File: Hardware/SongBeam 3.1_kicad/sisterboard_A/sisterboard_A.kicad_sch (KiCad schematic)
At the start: 59 parts, among them J1 RJ45, J2 Conn_01x04, U1 PCMD3180IRTWR, U10 LP5907MFX-1.8_NOPB, U2 IM66D132H, U3 IM66D132H, U4 IM66D132H, U5 IM66D132H, U6 IM66D132H, U7 IM66D132H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

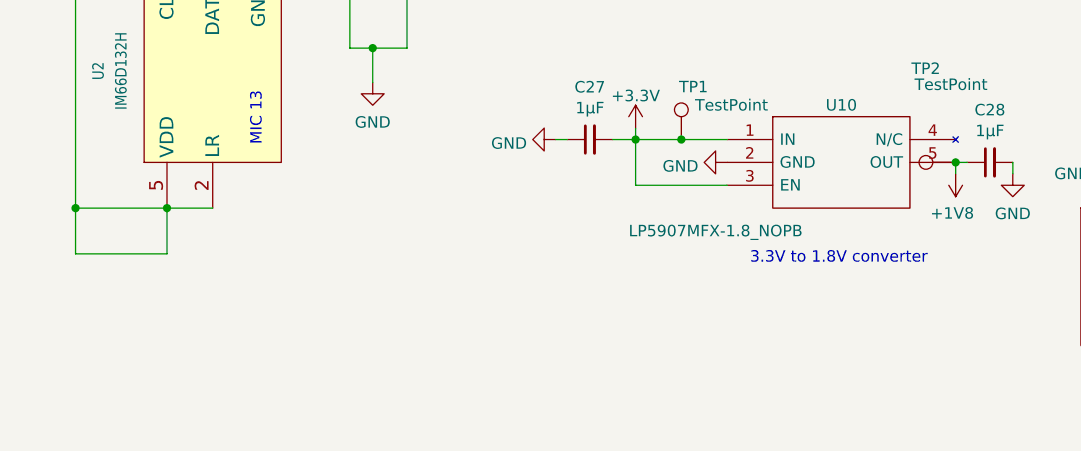
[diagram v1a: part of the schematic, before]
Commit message: Small tweaks, implementing the power modules
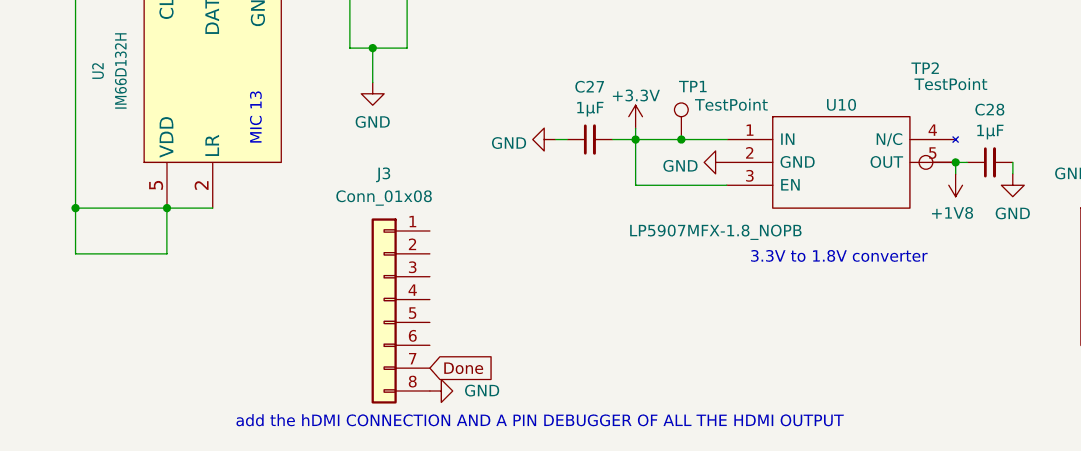
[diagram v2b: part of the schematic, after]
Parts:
- added J3: Conn_01x08, Connector_PinSocket_2.54mm:PinSocket_1x08_P2.54mm_Vertical, symbol Connector_Generic:Conn_01x08
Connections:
- net GND: now also J3.8 (Pin_8)
- new net Done: J3.7 (Pin_7)
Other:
- note added: "add the hDMI CONNECTION AND A PIN DEBUGGER OF ALL THE HDMI OUTPUT"
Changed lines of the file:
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@@
 		)
 	)
+	(text "add the hDMI CONNECTION AND A PIN DEBUGGER OF ALL THE HDMI OUTPUT\n"
+		(exclude_from_sim no)
+		(at 69.342 196.596 0)
+		(effects
+			(font
+				(size 1.27 1.27)
+			)
+		)
+	)
 	(text "MIC 11"
 		(exclude_from_sim no)
@@
 		)
 	)
+	(global_label "Done"
+		(shape input)
+		(at 57.15 190.5 0)
+		(fields_autoplaced yes)
+		(effects
+			(font
+				(size 1.27 1.27)
+			)
+			(justify left)
+		)
+		(property "Intersheetrefs" "${INTERSHEET_REFS}"
+			(at 64.7918 190.5 0)
+			(effects
+				(font
+					(size 1.27 1.27)
+				)
+				(justify left)
+				(hide yes)
+			)
+		)
+	)
 	(symbol
 		(lib_id "SoundRecorder_2.0:LP5907MFX-1.8_NOPB")
@@
 	)
 	(symbol
+		(lib_name "GND_2")
+		(lib_id "power:GND")
+		(at 57.15 193.04 90)
+		(unit 1)
+		(exclude_from_sim no)
+		(in_bom yes)
+		(on_board yes)
+		(dnp no)
+		(fields_autoplaced yes)
+		(property "Reference" "#PWR03"
+			(at 63.5 193.04 0)
+			(effects
+				(font
+					(size 1.27 1.27)
+				)
+				(hide yes)
+			)
+		)
+		(property "Value" "GND"
+			(at 60.96 193.0399 90)
+			(effects
+				(font
+					(size 1.27 1.27)
+				)
+				(justify right)
+			)
+		)
+		(property "Footprint" ""
+			(at 57.15 193.04 0)
+			(effects
+				(font
+					(size 1.27 1.27)
+				)
+				(hide yes)
+			)
+		)
+		(property "Datasheet" ""
+			(at 57.15 193.04 0)
+			(effects
+				(font
+					(size 1.27 1.27)
+				)
+				(hide yes)
+			)
+		)
+		(property "Description" "Power symbol creates a global label with name \"GND\" , ground"
+			(at 57.15 193.04 0)
+			(effects
+				(font
+					(size 1.27 1.27)
+				)
+				(hide yes)
+			)
+		)
+		(pin "1"
+		)
+		(instances
+			(project "sisterboard_A"
+				(path "/4ef09cdb-8bcc-4078-80cc-bd6392fd6a14"
+					(reference "#PWR03")
+					(unit 1)
+				)
+			)
+		)
+	)
+	(symbol
 		(lib_id "power:GND")
 		(at 137.16 54.61 90)
@@
 					(unit 1)
 				)
+			)
+		)
+	)
+	(symbol
+		(lib_id "Connector_Generic:Conn_01x08")
+		(at 52.07 182.88 0)
+		(mirror y)
+		(unit 1)
+		(exclude_from_sim no)
+		(in_bom yes)
+		(on_board yes)
+		(dnp no)
+		(fields_autoplaced yes)
+		(property "Reference" "J3"
+			(at 52.07 168.91 0)
+			(effects
+				(font
+					(size 1.27 1.27)
+				)
+			)
+		)
+		(property "Value" "Conn_01x08"
+			(at 52.07 171.45 0)
+			(effects
+				(font
+					(size 1.27 1.27)
+				)
+			)
+		)
+		(property "Footprint" "Connector_PinSocket_2.54mm:PinSocket_1x08_P2.54mm_Vertical"
+			(at 52.07 182.88 0)
+			(effects
+				(font
+					(size 1.27 1.27)
+				)
+				(hide yes)
+			)
+		)
+		(property "Datasheet" "~"
+			(at 52.07 182.88 0)
+			(effects
+				(font
+					(size 1.27 1.27)
+				)
+				(hide yes)
+			)
+		)
+		(property "Description" ""
+			(at 52.07 182.88 0)
+			(effects
+				(font
+					(size 1.27 1.27)
+				)
+			)
+		)
+		(pin "1"
+		)
+		(pin "2"
+		)
+		(pin "3"
+		)
+		(pin "4"
+		)
+		(pin "5"
+		)
+		(pin "6"
+		)
+		(pin "7"
+		)
+		(pin "8"
+		)
+		(instances
+			(project "sisterboard_A"
+				(path "/4ef09cdb-8bcc-4078-80cc-bd6392fd6a14"
+					(reference "J3")
+					(unit 1)
+				)
